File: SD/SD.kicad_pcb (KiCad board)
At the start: 2 copper layers, 49.5 x 42.5 mm, 17 parts, among them J1 PMOD1, J2 SD_Card

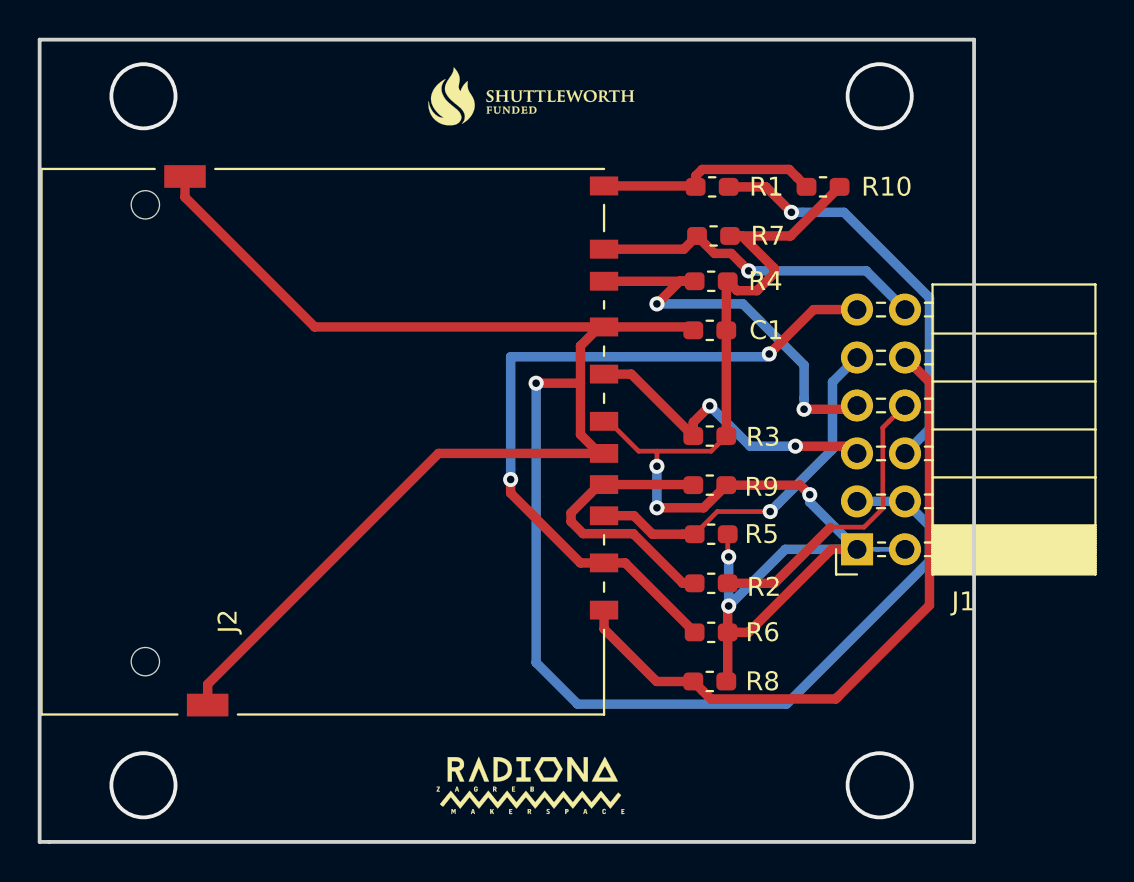
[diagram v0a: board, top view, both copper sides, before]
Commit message: Fixing pinouts and pictures
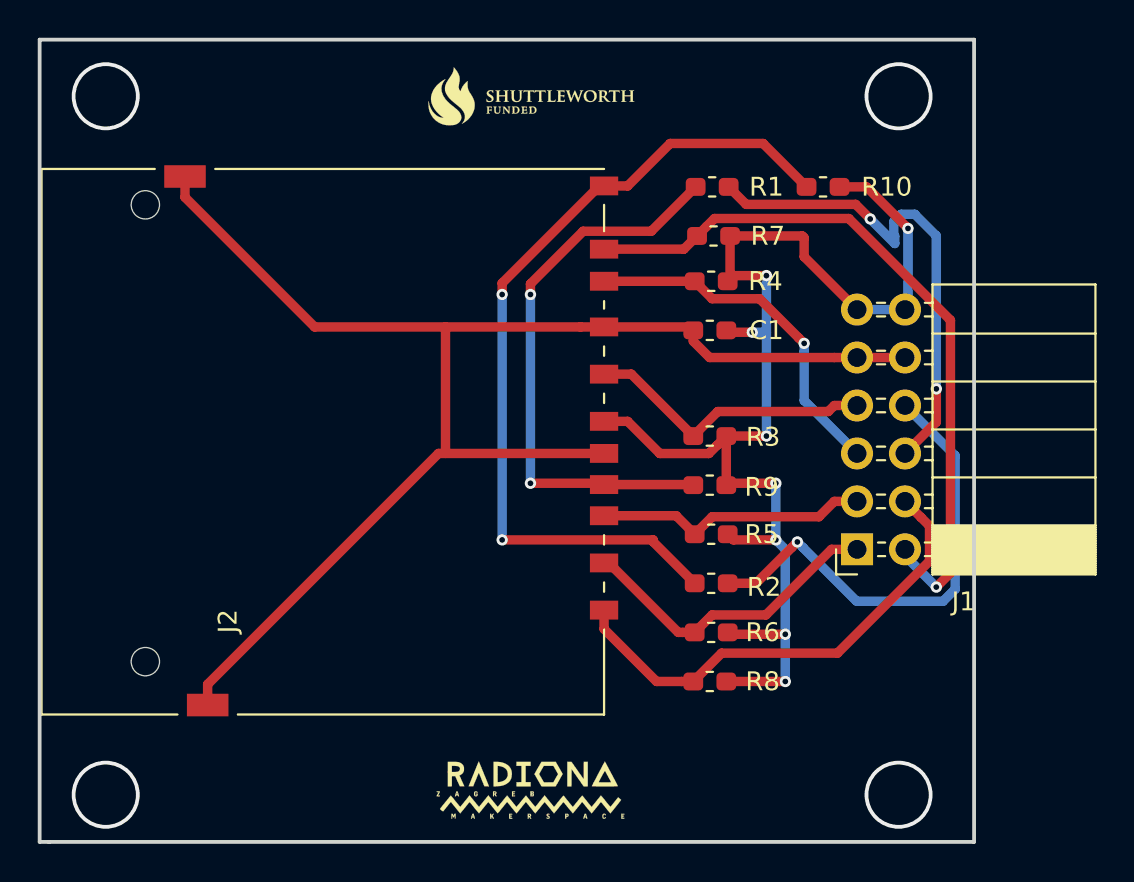
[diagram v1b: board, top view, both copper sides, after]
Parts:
- moved G*** 0.25 mm to (141.5, 89.8)
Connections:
- J1 pad 1: 3V3 -> CS
- J1 pad 10: DAT2 -> GND
- J1 pad 11: CS -> 3V3
- J1 pad 12: DAT1 -> 3V3
- J1 pad 2: 3V3 -> DAT1
- J1 pad 3: GND -> MOSI
- J1 pad 4: GND -> DAT2
- J1 pad 5: SCK -> MISO
- J1 pad 7: MISO -> SCK
- J1 pad 9: MOSI -> GND
- R1 pad 1: WP -> CD
- R2 pad 2: CD -> WP
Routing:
- net GND: track 114.4 -> 77.0 mm, vias 1 -> 0
- net WP: track 11.8 -> 45.0 mm, vias 0 -> 2
- net CS: track 39.4 -> 16.7 mm, vias 2 -> 0
- net DAT1: track 17.8 -> 38.4 mm
- net CD: track 15.5 -> 30.1 mm, vias 0 -> 2
- net DAT2: track 35.5 -> 25.7 mm
- net Net-(J1-Pad8): track 15.8 -> 25.4 mm, vias 0 -> 1
- net MOSI: track 19.8 -> 14.5 mm, vias 1 -> 0
- net Net-(J1-Pad6): track 21.9 -> 26.3 mm, vias 1 -> 2
- net 3V3: track 73.3 -> 70.2 mm, vias 5 -> 8
- net MISO: track 21.7 -> 19.0 mm, vias 2 -> 1
- net SCK: track 16.9 -> 15.4 mm, vias 2 -> 0

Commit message: New versions
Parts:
- moved G*** 3.29 mm to (144.8, 53.5)
- moved G*** 1.82 mm to (140.2, 88.5)
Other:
- outline, holes or cut-outs redrawn
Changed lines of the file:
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@@
   (general
     (thickness 1.6)
-    (drawings 17)
+    (drawings 20)
     (tracks 164)
     (zones 0)
@@
   (page A4)
   (layers
-    (0 F.Cu signal hide)
-    (31 B.Cu signal hide)
+    (0 F.Cu signal)
+    (31 B.Cu signal)
     (32 B.Adhes user)
     (33 F.Adhes user)
@@
   )
   (setup
-    (last_trace_width 0.5)
+    (last_trace_width 0.25)
     (user_trace_width 0.5)
     (user_trace_width 0.75)
@@
       (layerselection 0x010fc_ffffffff)
       (usegerberextensions false)
-      (usegerberattributes false)
-      (usegerberadvancedattributes false)
+      (usegerberattributes true)
+      (usegerberadvancedattributes true)
       (creategerberjobfile false)
       (excludeedgelayer true)
@@
       (outputformat 1)
       (mirror false)
-      (drillshape 1)
+      (drillshape 0)
       (scaleselection 1)
-      (outputdirectory ""))
+      (outputdirectory "Gerber/"))
   )
   (net 0 "")
@@
   )
   (module parts:radiona-16mm (layer B.Cu)
-    (at 141.5 54)
+    (at 144.75 53.5)
     (fp_text reference G*** (at 0 0) (layer B.SilkS) hide
       (effects (font (size 1.524 1.524) (thickness 0.3)) (justify mirror))
@@
   )
   (module parts:shutleworth (layer B.Cu)
-    (at 142 88)
+    (at 140.25 88.5)
     (fp_text reference G*** (at 0 0) (layer B.SilkS) hide
       (effects (font (size 1.524 1.524) (thickness 0.3)) (justify mirror))
@@
       (xy -4.18592 1.25984) (xy -4.151381 1.25984) (xy -4.130649 1.261396)) (layer F.SilkS) (width 0.01))
   )
+  (gr_line (start 133.25 50) (end 115.5 50) (layer Edge.Cuts) (width 0.15))
+  (gr_line (start 165 50) (end 136.75 50) (layer Edge.Cuts) (width 0.15))
+  (gr_line (start 136.75 92.5) (end 165 92.5) (layer Edge.Cuts) (width 0.15))
+  (gr_line (start 115.5 92.5) (end 133.25 92.5) (layer Edge.Cuts) (width 0.15))
+  (gr_arc (start 135 92.5) (end 136.75 92.5) (angle -180) (layer Edge.Cuts) (width 0.15))
+  (gr_arc (start 135 50) (end 133.25 50) (angle -180) (layer Edge.Cuts) (width 0.15))
   (gr_text 3V3 (at 161.25 65.5 180) (layer B.SilkS)
     (effects (font (size 0.5 0.5) (thickness 0.1)) (justify mirror))
   )
   (gr_line (start 115.5 92.5) (end 115.5 50) (layer Edge.Cuts) (width 0.2))
-  (gr_line (start 116 92.5) (end 115.5 92.5) (layer Edge.Cuts) (width 0.2))
-  (gr_line (start 165 92.5) (end 116 92.5) (layer Edge.Cuts) (width 0.2))
   (gr_line (start 165 50) (end 165 92.5) (layer Edge.Cuts) (width 0.2))
-  (gr_line (start 115.5 50) (end 165 50) (layer Edge.Cuts) (width 0.2))
   (gr_text CS (at 158.75 78.5 180) (layer B.SilkS)
     (effects (font (size 0.5 0.5) (thickness 0.1)) (justify mirror))
@@
     (polygon
       (pts
-        (xy 115.5 50) (xy 165 50) (xy 165 92.5) (xy 115.5 92.5)
+        (xy 165 50) (xy 165 92.5) (xy 115.5 92.5) (xy 115.5 50)
       )
     )
@@
     (polygon
       (pts
-        (xy 165 92.5) (xy 165 50) (xy 115.5 50) (xy 115.5 92.5)
+        (xy 165 50) (xy 115.5 50) (xy 115.5 92.5) (xy 165 92.5)
       )
     )
